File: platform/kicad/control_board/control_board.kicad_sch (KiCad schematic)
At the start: 32 parts, among them J1 DHT22, J10 ADC1,7, J11 Qwiic JST, J12 Data 1, J13 Data 2, J16 Data 3, J17 PoE 2, J2 DS18B20, J5 Conn_01x05_Pin, J6 PoE 1, J7 PoE 3, J8 UART, J9 ADC1,6, U1 ESP32-DevKitC

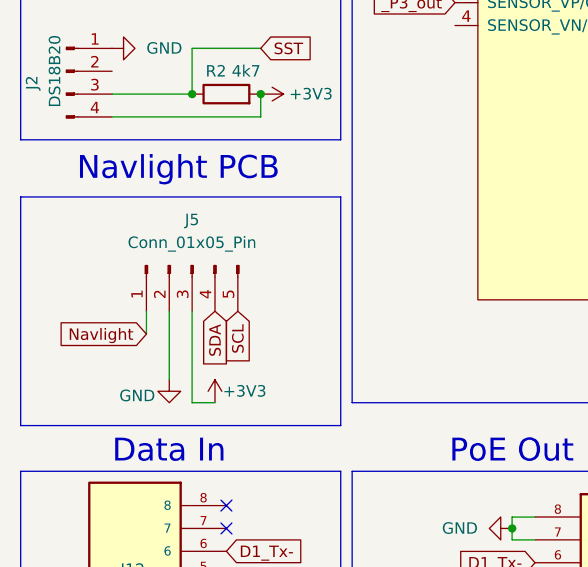
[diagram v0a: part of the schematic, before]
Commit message: Controller PCB: Update connector positions (#21)
This change slightly alters the positioning of some connectors to increase the usability of the board.
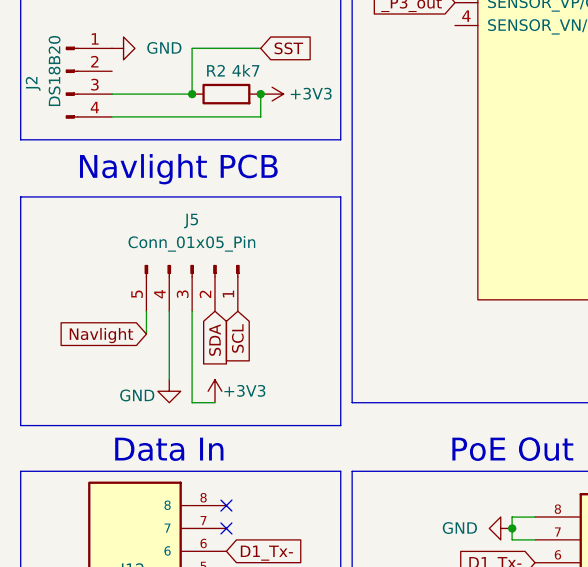
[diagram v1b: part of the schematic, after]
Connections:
- net GND: now also J5.4 (Pin_4); no longer J5.2 (Pin_2)
- net Navlight: now also J5.5 (Pin_5); no longer J5.1 (Pin_1)
- net SCL: now also J5.1 (Pin_1); no longer J5.5 (Pin_5)
- net SDA: now also J5.2 (Pin_2); no longer J5.4 (Pin_4)
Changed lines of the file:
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@@
+	)
+	(symbol
+		(lib_id "Connector:Conn_01x05_Pin")
+		(at 33.02 92.71 270)
+		(unit 1)
+		(exclude_from_sim no)
+		(in_bom yes)
+		(on_board yes)
+		(dnp no)
+		(property "Reference" "J5"
+			(at 33.02 87.63 90)
+			(effects
+				(font
+					(size 1.27 1.27)
+				)
+			)
+		)
+		(property "Value" "Conn_01x05_Pin"
+			(at 33.02 90.17 90)
+			(effects
+				(font
+					(size 1.27 1.27)
+				)
+			)
+		)
+		(property "Footprint" "Connector_JST:JST_SH_SM05B-SRSS-TB_1x05-1MP_P1.00mm_Horizontal"
+			(at 33.02 92.71 0)
+			(effects
+				(font
+					(size 1.27 1.27)
+				)
+				(hide yes)
+			)
+		)
+		(property "Datasheet" "~"
+			(at 33.02 92.71 0)
+			(effects
+				(font
+					(size 1.27 1.27)
+				)
+				(hide yes)
+			)
+		)
+		(property "Description" "Generic connector, single row, 01x05, script generated"
+			(at 33.02 92.71 0)
+			(effects
+				(font
+					(size 1.27 1.27)
+				)
+				(hide yes)
+			)
+		)
+		(pin "4"
+		)
+		(pin "5"
+		)
+		(pin "3"
+		)
+		(pin "2"
+		)
+		(pin "1"
+		)
+		(instances
+			(project "control_board"
+				(path "/bacab6d6-2a0b-4208-9256-c826bcae29b3"
+					(reference "J5")
+					(unit 1)
+				)
+			)
+		)
 	)
 	(symbol
@@
 					(unit 1)
 				)
-			)
-		)
-	)
-	(symbol
-		(lib_id "Connector:Conn_01x05_Pin")
-		(at 33.02 92.71 90)
-		(mirror x)
-		(unit 1)
-		(exclude_from_sim no)
-		(in_bom yes)
-		(on_board yes)
-		(dnp no)
-		(property "Reference" "J5"
-			(at 33.02 87.63 90)
-			(effects
-				(font
-					(size 1.27 1.27)
-				)
-			)
-		)
-		(property "Value" "Conn_01x05_Pin"
-			(at 33.02 90.17 90)
-			(effects
-				(font
-					(size 1.27 1.27)
-				)
-			)
-		)
-		(property "Footprint" "Connector_JST:JST_SH_SM05B-SRSS-TB_1x05-1MP_P1.00mm_Horizontal"
-			(at 33.02 92.71 0)
-			(effects
-				(font
-					(size 1.27 1.27)
-				)
-				(hide yes)
-			)
-		)
-		(property "Datasheet" "~"
-			(at 33.02 92.71 0)
-			(effects
-				(font
-					(size 1.27 1.27)
-				)
-				(hide yes)
-			)
-		)
-		(property "Description" "Generic connector, single row, 01x05, script generated"
-			(at 33.02 92.71 0)
-			(effects
-				(font
-					(size 1.27 1.27)
-				)
-				(hide yes)
-			)
-		)
-		(pin "4"
-		)
-		(pin "5"
-		)
-		(pin "3"
-		)
-		(pin "2"
-		)
-		(pin "1"
-		)
-		(instances
-			(project "control_board"
-				(path "/bacab6d6-2a0b-4208-9256-c826bcae29b3"
-					(reference "J5")
-					(unit 1)
-				)

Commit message: Controller: Upsize resistors
This change alters the resistor footprints from 0201 to 0603 which allows the cheaper
PCBA method to be used, decreasing the cost of the board.
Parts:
- R1, R10, R11, R12, R19, R2, R20, R21, R3, R4, R5, R6, R7, R8, R9: footprint Resistor_SMD:R_0201_0603Metric -> Resistor_SMD:R_0603_1608Metric
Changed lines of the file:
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@@
 			)
 		)
-		(property "Footprint" "Resistor_SMD:R_0201_0603Metric"
+		(property "Footprint" "Resistor_SMD:R_0603_1608Metric"
 			(at 159.512 31.75 90)
 			(effects
@@
 			)
 		)
-		(property "Footprint" "Resistor_SMD:R_0201_0603Metric"
+		(property "Footprint" "Resistor_SMD:R_0603_1608Metric"
 			(at 198.882 31.75 90)
 			(effects
@@
 			)
 		)
-		(property "Footprint" "Resistor_SMD:R_0201_0603Metric"
+		(property "Footprint" "Resistor_SMD:R_0603_1608Metric"
 			(at 159.512 68.58 90)
 			(effects
@@
 			)
 		)
-		(property "Footprint" "Resistor_SMD:R_0201_0603Metric"
+		(property "Footprint" "Resistor_SMD:R_0603_1608Metric"
 			(at 159.512 60.96 90)
 			(effects
@@
 			)
 		)
-		(property "Footprint" "Resistor_SMD:R_0201_0603Metric"
+		(property "Footprint" "Resistor_SMD:R_0603_1608Metric"
 			(at 177.292 31.75 90)
 			(effects
@@
 			)
 		)
-		(property "Footprint" "Resistor_SMD:R_0201_0603Metric"
+		(property "Footprint" "Resistor_SMD:R_0603_1608Metric"
 			(at 177.292 68.58 90)
 			(effects
@@
 			)
 		)
-		(property "Footprint" "Resistor_SMD:R_0201_0603Metric"
+		(property "Footprint" "Resistor_SMD:R_0603_1608Metric"
 			(at 177.292 60.96 90)
 			(effects
@@
 			)
 		)
-		(property "Footprint" "Resistor_SMD:R_0201_0603Metric"
+		(property "Footprint" "Resistor_SMD:R_0603_1608Metric"
 			(at 177.292 39.37 90)
 			(effects
@@
 			)
 		)
-		(property "Footprint" "Resistor_SMD:R_0201_0603Metric"
+		(property "Footprint" "Resistor_SMD:R_0603_1608Metric"
 			(at 198.882 39.37 90)
 			(effects
@@
 			)
 		)
-		(property "Footprint" "Resistor_SMD:R_0201_0603Metric"
+		(property "Footprint" "Resistor_SMD:R_0603_1608Metric"
 			(at 134.62 168.91 0)
 			(effects
@@
 			)
 		)
-		(property "Footprint" "Resistor_SMD:R_0201_0603Metric"
+		(property "Footprint" "Resistor_SMD:R_0603_1608Metric"
 			(at 134.62 162.56 0)
 			(effects
@@
 			)
 		)
-		(property "Footprint" "Resistor_SMD:R_0201_0603Metric"
+		(property "Footprint" "Resistor_SMD:R_0603_1608Metric"
 			(at 36.83 75.438 90)
 			(effects
@@
 			)
 		)
-		(property "Footprint" "Resistor_SMD:R_0201_0603Metric"
+		(property "Footprint" "Resistor_SMD:R_0603_1608Metric"
 			(at 36.83 60.198 90)
 			(effects
@@
 			)
 		)
-		(property "Footprint" "Resistor_SMD:R_0201_0603Metric"
+		(property "Footprint" "Resistor_SMD:R_0603_1608Metric"
 			(at 134.62 175.26 0)
 			(effects
@@
 			)
 		)
-		(property "Footprint" "Resistor_SMD:R_0201_0603Metric"
+		(property "Footprint" "Resistor_SMD:R_0603_1608Metric"
 			(at 159.512 39.37 90)
 			(effects
